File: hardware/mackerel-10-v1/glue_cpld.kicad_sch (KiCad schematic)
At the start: 20 parts, among them J1 Conn_02x05_Odd_Even, J7 Conn_02x03_Odd_Even, X1 50MHz, X2 50MHz

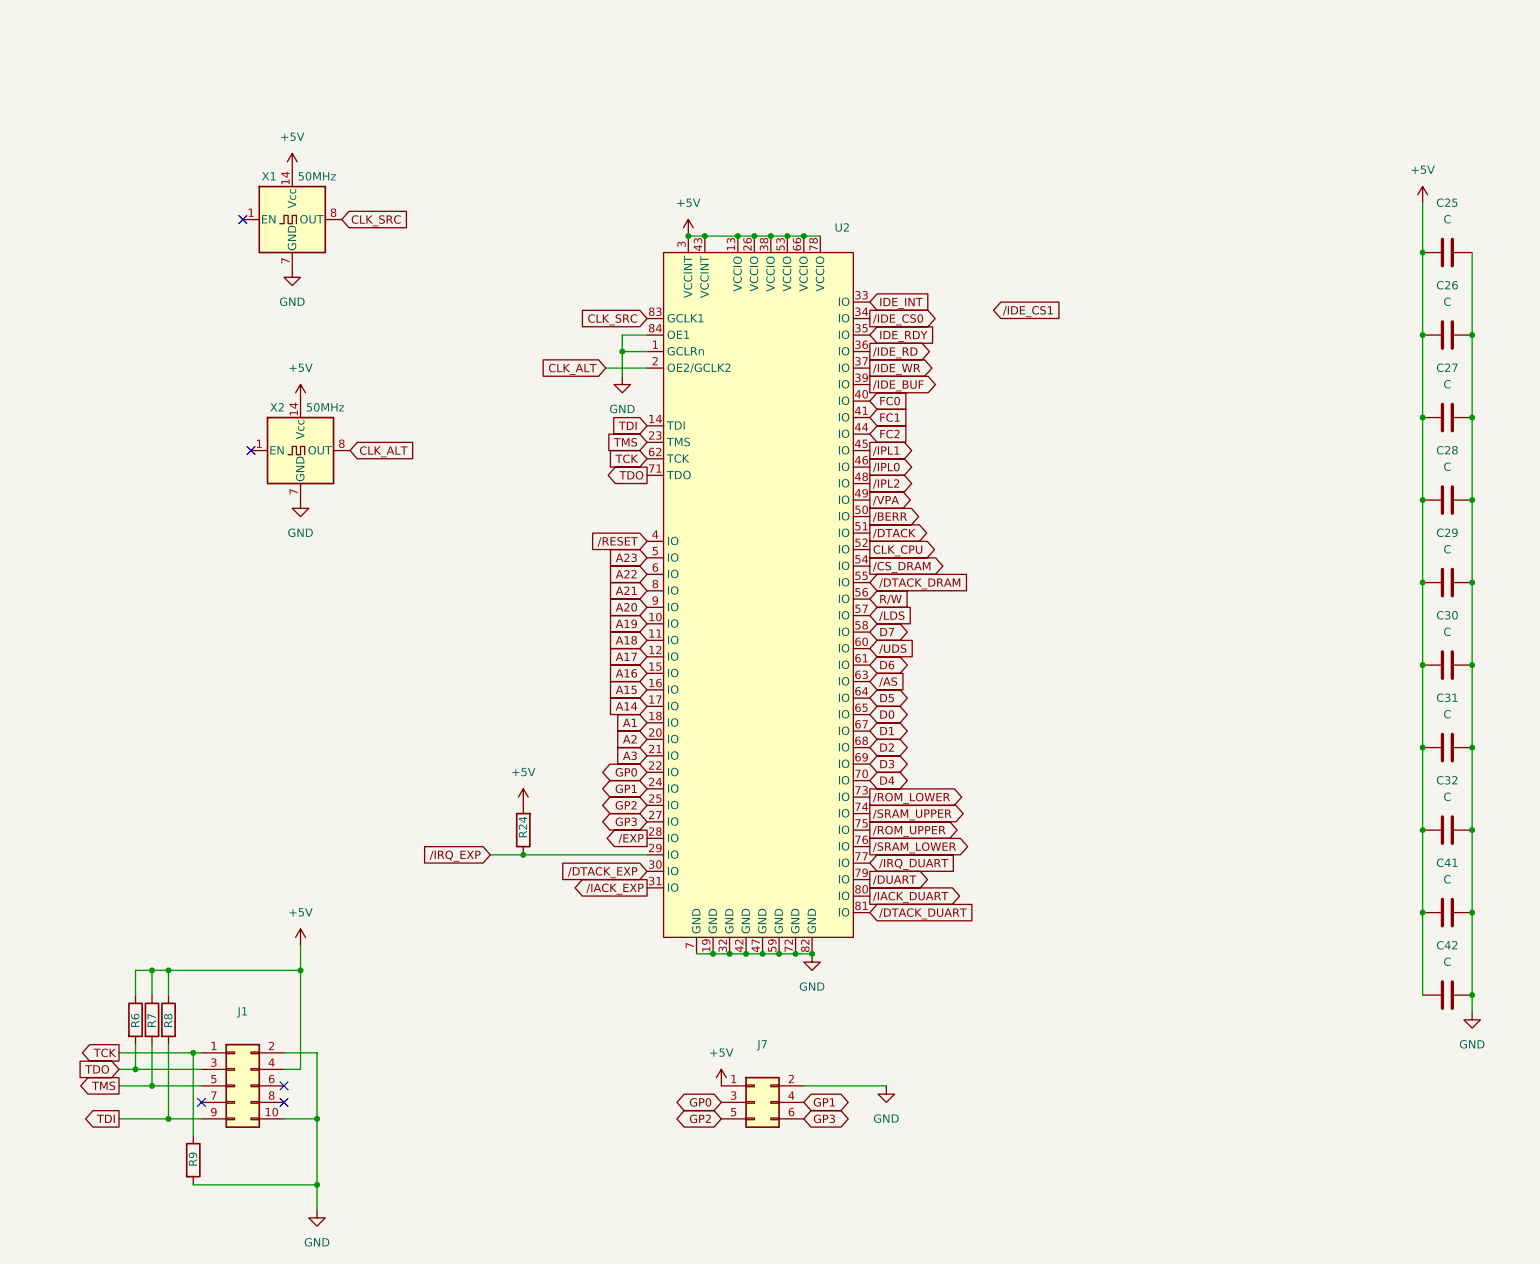
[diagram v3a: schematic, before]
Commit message: Remove BERR from CPLD
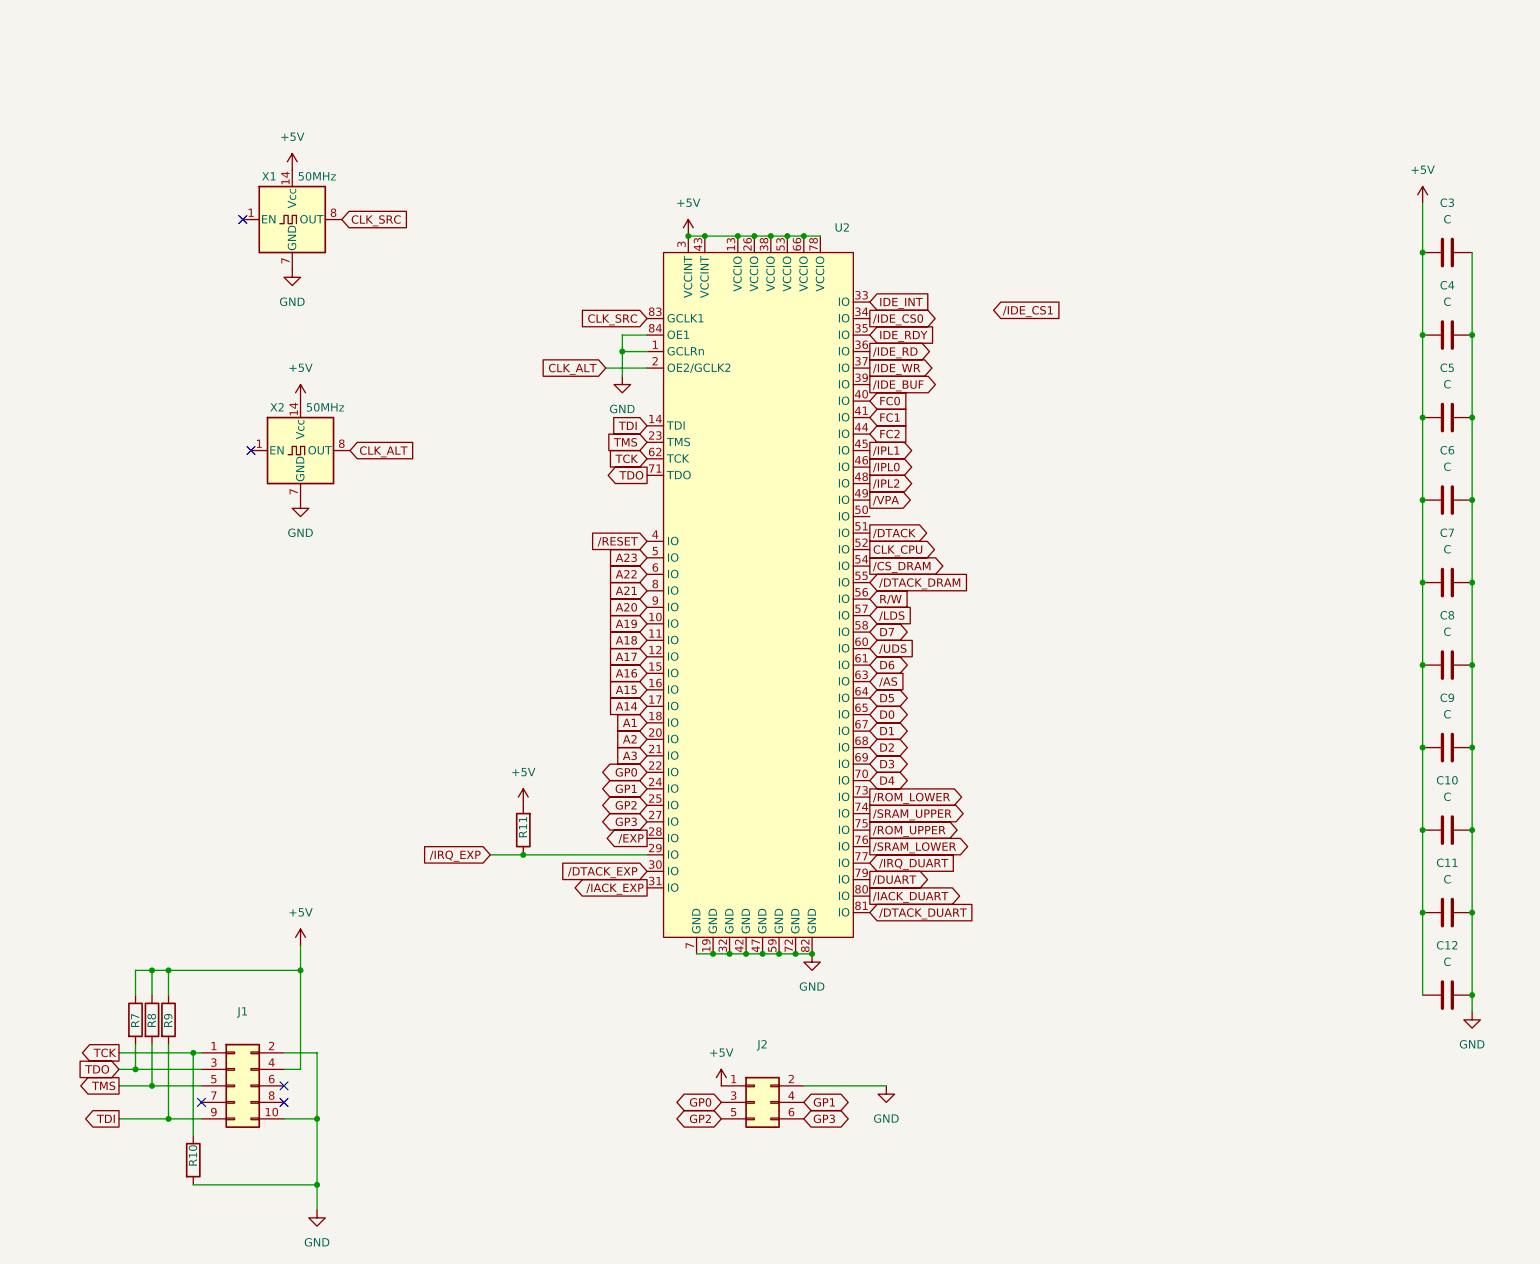
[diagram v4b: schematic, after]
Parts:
- renumbered C32 to C10, C41 to C11, C42 to C12, C25 to C3, C26 to C4, C27 to C5, C28 to C6, C29 to C7, C30 to C8, C31 to C9, J7 to J2, R9 to R10, R24 to R11, R6 to R7, R7 to R8, R8 to R9
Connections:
- net /BERR: no longer names the net of U2.50 (IO)
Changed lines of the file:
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@@
 		)
 	)
-	(global_label "{slash}BERR"
-		(shape output)
-		(at 147.32 81.28 0)
-		(fields_autoplaced yes)
-		(effects
-			(font
-				(size 1.27 1.27)
-			)
-			(justify left)
-		)
-		(property "Intersheetrefs" "${INTERSHEET_REFS}"
-			(at 156.5947 81.28 0)
-			(effects
-				(font
-					(size 1.27 1.27)
-				)
-				(justify left)
-				(hide yes)
-			)
-		)
-	)
 	(global_label "TDI"
 		(shape input)
@@
 		(dnp no)
 		(fields_autoplaced yes)
-		(property "Reference" "#PWR04"
+		(property "Reference" "#PWR010"
 			(at 62.23 194.31 0)
 			(effects
@@
 			(project "mackerel-10-v1"
 				(path "/0a8f74be-008b-4256-a2d9-73a458311ea0/ffc18f07-5f09-466c-bd63-a2a9c38b4664"
-					(reference "#PWR04")
+					(reference "#PWR010")
 					(unit 1)
 				)
@@
 		(dnp no)
 		(fields_autoplaced yes)
-		(property "Reference" "#PWR082"
+		(property "Reference" "#PWR08"
 			(at 59.69 85.09 0)
 			(effects
@@
 			(project "mackerel-10-v1"
 				(path "/0a8f74be-008b-4256-a2d9-73a458311ea0/ffc18f07-5f09-466c-bd63-a2a9c38b4664"
-					(reference "#PWR082")
+					(reference "#PWR08")
 					(unit 1)
 				)
@@
 		(dnp no)
 		(fields_autoplaced yes)
-		(property "Reference" "C26"
+		(property "Reference" "C4"
 			(at 236.22 45.72 90)
 			(effects
@@
 			(project "mackerel-10-v1"
 				(path "/0a8f74be-008b-4256-a2d9-73a458311ea0/ffc18f07-5f09-466c-bd63-a2a9c38b4664"
-					(reference "C26")
+					(reference "C4")
 					(unit 1)
 				)
@@
 		(on_board yes)
 		(dnp no)
-		(property "Reference" "R6"
+		(property "Reference" "R7"
 			(at 34.29 160.02 90)
 			(effects
@@
 			(project "mackerel-10-v1"
 				(path "/0a8f74be-008b-4256-a2d9-73a458311ea0/ffc18f07-5f09-466c-bd63-a2a9c38b4664"
-					(reference "R6")
+					(reference "R7")
 					(unit 1)
 				)
@@
 		(dnp no)
 		(fields_autoplaced yes)
-		(property "Reference" "#PWR067"
+		(property "Reference" "#PWR016"
 			(at 149.86 175.26 0)
 			(effects
@@
 			(project "mackerel-10-v1"
 				(path "/0a8f74be-008b-4256-a2d9-73a458311ea0/ffc18f07-5f09-466c-bd63-a2a9c38b4664"
-					(reference "#PWR067")
+					(reference "#PWR016")
 					(unit 1)
 				)
@@
 		(dnp no)
 		(fields_autoplaced yes)
-		(property "Reference" "C42"
+		(property "Reference" "C12"
 			(at 236.22 147.32 90)
 			(effects
@@
 			(project "mackerel-10-v1"
 				(path "/0a8f74be-008b-4256-a2d9-73a458311ea0/ffc18f07-5f09-466c-bd63-a2a9c38b4664"
-					(reference "C42")
+					(reference "C12")
 					(unit 1)
 				)
@@
 		(dnp no)
 		(fields_autoplaced yes)
-		(property "Reference" "#PWR09"
+		(property "Reference" "#PWR015"
 			(at 138.43 154.94 0)
 			(effects
@@
 			(project "mackerel-10-v1"
 				(path "/0a8f74be-008b-4256-a2d9-73a458311ea0/ffc18f07-5f09-466c-bd63-a2a9c38b4664"
-					(reference "#PWR09")
+					(reference "#PWR015")
 					(unit 1)
 				)
@@
 		(dnp no)
 		(fields_autoplaced yes)
-		(property "Reference" "#PWR088"
+		(property "Reference" "#PWR017"
 			(at 232.41 36.83 0)
 			(effects
@@
 			(project "mackerel-10-v1"
 				(path "/0a8f74be-008b-4256-a2d9-73a458311ea0/ffc18f07-5f09-466c-bd63-a2a9c38b4664"
-					(reference "#PWR088")
+					(reference "#PWR017")
 					(unit 1)
 				)
@@
 		(on_board yes)
 		(dnp no)
-		(property "Reference" "R7"
+		(property "Reference" "R8"
 			(at 36.83 160.02 90)
 			(effects
@@
 			(project "mackerel-10-v1"
 				(path "/0a8f74be-008b-4256-a2d9-73a458311ea0/ffc18f07-5f09-466c-bd63-a2a9c38b4664"
-					(reference "R7")
+					(reference "R8")
 					(unit 1)
 				)
@@
 		(dnp no)
 		(fields_autoplaced yes)
-		(property "Reference" "#PWR0116"
+		(property "Reference" "#PWR011"
 			(at 93.98 129.54 0)
 			(effects
@@
 			(project "mackerel-10-v1"
 				(path "/0a8f74be-008b-4256-a2d9-73a458311ea0/ffc18f07-5f09-466c-bd63-a2a9c38b4664"
-					(reference "#PWR0116")
+					(reference "#PWR011")
 					(unit 1)
 				)
@@
 		(dnp no)
 		(fields_autoplaced yes)
-		(property "Reference" "C28"
+		(property "Reference" "C6"
 			(at 236.22 71.12 90)
 			(effects
@@
 			(project "mackerel-10-v1"
 				(path "/0a8f74be-008b-4256-a2d9-73a458311ea0/ffc18f07-5f09-466c-bd63-a2a9c38b4664"
-					(reference "C28")
+					(reference "C6")
 					(unit 1)
 				)
@@
 		(dnp no)
 		(fields_autoplaced yes)
-		(property "Reference" "C25"
+		(property "Reference" "C3"
 			(at 236.22 33.02 90)
 			(effects
@@
 			(project "mackerel-10-v1"
 				(path "/0a8f74be-008b-4256-a2d9-73a458311ea0/ffc18f07-5f09-466c-bd63-a2a9c38b4664"
-					(reference "C25")
+					(reference "C3")
 					(unit 1)
 				)
@@
 		(on_board yes)
 		(dnp no)
-		(property "Reference" "R24"
+		(property "Reference" "R11"
 			(at 93.98 130.81 90)
 			(effects
@@
 			(project "mackerel-10-v1"
 				(path "/0a8f74be-008b-4256-a2d9-73a458311ea0/ffc18f07-5f09-466c-bd63-a2a9c38b4664"
-					(reference "R24")
+					(reference "R11")
 					(unit 1)
 				)
@@
 		(dnp no)
 		(fields_autoplaced yes)
-		(property "Reference" "J7"
+		(property "Reference" "J2"
 			(at 130.81 162.56 0)
 			(effects
@@
 			(project ""
 				(path "/0a8f74be-008b-4256-a2d9-73a458311ea0/ffc18f07-5f09-466c-bd63-a2a9c38b4664"
-					(reference "J7")
+					(reference "J2")
 					(unit 1)
 				)
@@
 		(on_board yes)
 		(dnp no)
-		(property "Reference" "R8"
+		(property "Reference" "R9"
 			(at 39.37 160.02 90)
 			(effects
@@
 			(project "mackerel-10-v1"
 				(path "/0a8f74be-008b-4256-a2d9-73a458311ea0/ffc18f07-5f09-466c-bd63-a2a9c38b4664"
-					(reference "R8")
+					(reference "R9")
 					(unit 1)
 				)
@@
 		(dnp no)
 		(fields_autoplaced yes)
-		(property "Reference" "C41"
+		(property "Reference" "C11"
 			(at 236.22 134.62 90)
 			(effects
@@
 			(project "mackerel-10-v1"
 				(path "/0a8f74be-008b-4256-a2d9-73a458311ea0/ffc18f07-5f09-466c-bd63-a2a9c38b4664"
-					(reference "C41")
+					(reference "C11")
 					(unit 1)
 				)
@@
 		(dnp no)
 		(fields_autoplaced yes)
-		(property "Reference" "#PWR03"
+		(property "Reference" "#PWR09"
 			(at 59.69 151.13 0)
 			(effects
@@
 			(project "mackerel-10-v1"
 				(path "/0a8f74be-008b-4256-a2d9-73a458311ea0/ffc18f07-5f09-466c-bd63-a2a9c38b4664"
-					(reference "#PWR03")
+					(reference "#PWR09")
 					(unit 1)
 				)
@@
 		(dnp no)
 		(fields_autoplaced yes)
-		(property "Reference" "#PWR068"
+		(property "Reference" "#PWR014"
 			(at 124.46 172.72 0)
 			(effects
@@
 			(project "mackerel-10-v1"
 				(path "/0a8f74be-008b-4256-a2d9-73a458311ea0/ffc18f07-5f09-466c-bd63-a2a9c38b4664"
-					(reference "#PWR068")
+					(reference "#PWR014")
 					(unit 1)
 				)
@@
 		(dnp no)
 		(fields_autoplaced yes)
-		(property "Reference" "C32"
+		(property "Reference" "C10"
 			(at 236.22 121.92 90)
 			(effects
@@
 			(project "mackerel-10-v1"
 				(path "/0a8f74be-008b-4256-a2d9-73a458311ea0/ffc18f07-5f09-466c-bd63-a2a9c38b4664"
-					(reference "C32")
+					(reference "C10")
 					(unit 1)
 				)
@@
 		(dnp no)
 		(fields_autoplaced yes)
-		(property "Reference" "#PWR08"
+		(property "Reference" "#PWR013"
 			(at 119.38 41.91 0)
 			(effects
@@
 			(project "mackerel-10-v1"
 				(path "/0a8f74be-008b-4256-a2d9-73a458311ea0/ffc18f07-5f09-466c-bd63-a2a9c38b4664"
-					(reference "#PWR08")
+					(reference "#PWR013")
 					(unit 1)
 				)
@@
 		(dnp no)
 		(fields_autoplaced yes)
-		(property "Reference" "#PWR07"
+		(property "Reference" "#PWR012"
 			(at 109.22 66.04 0)
 			(effects
@@
 			(project "mackerel-10-v1"
 				(path "/0a8f74be-008b-4256-a2d9-73a458311ea0/ffc18f07-5f09-466c-bd63-a2a9c38b4664"
-					(reference "#PWR07")
+					(reference "#PWR012")
 					(unit 1)
 				)
@@
 		(dnp no)
 		(fields_autoplaced yes)
-		(property "Reference" "#PWR092"
+		(property "Reference" "#PWR018"
 			(at 240.03 163.83 0)
 			(effects
@@
 			(project "mackerel-10-v1"
 				(path "/0a8f74be-008b-4256-a2d9-73a458311ea0/ffc18f07-5f09-466c-bd63-a2a9c38b4664"
-					(reference "#PWR092")
+					(reference "#PWR018")
 					(unit 1)
 				)
@@
 		(dnp no)
 		(fields_autoplaced yes)
-		(property "Reference" "C31"
+		(property "Reference" "C9"
 			(at 236.22 109.22 90)
 			(effects
@@
 			(project "mackerel-10-v1"
 				(path "/0a8f74be-008b-4256-a2d9-73a458311ea0/ffc18f07-5f09-466c-bd63-a2a9c38b4664"
-					(reference "C31")
+					(reference "C9")
 					(unit 1)
 				)
@@
 		(on_board yes)
 		(dnp no)
-		(property "Reference" "R9"
+		(property "Reference" "R10"
 			(at 43.18 181.356 90)
 			(effects
@@
 			(project "mackerel-10-v1"
 				(path "/0a8f74be-008b-4256-a2d9-73a458311ea0/ffc18f07-5f09-466c-bd63-a2a9c38b4664"
-					(reference "R9")
+					(reference "R10")
 					(unit 1)
 				)
@@
 		(dnp no)
 		(fields_autoplaced yes)
-		(property "Reference" "C30"
+		(property "Reference" "C8"
 			(at 236.22 96.52 90)
 			(effects
@@
 			(project "mackerel-10-v1"
 				(path "/0a8f74be-008b-4256-a2d9-73a458311ea0/ffc18f07-5f09-466c-bd63-a2a9c38b4664"
-					(reference "C30")
+					(reference "C8")
 					(unit 1)
 				)
@@
 		(on_board yes)
 		(dnp no)
-		(property "Reference" "C27"
+		(property "Reference" "C5"
 			(at 236.22 58.42 90)
 			(effects
@@
 			(project "mackerel-10-v1"
 				(path "/0a8f74be-008b-4256-a2d9-73a458311ea0/ffc18f07-5f09-466c-bd63-a2a9c38b4664"
-					(reference "C27")
+					(reference "C5")
 					(unit 1)
 				)
@@
 		(dnp no)
 		(fields_autoplaced yes)
-		(property "Reference" "#PWR081"
+		(property "Reference" "#PWR07"
 			(at 59.69 67.31 0)
 			(effects
@@
 			(project "mackerel-10-v1"
 				(path "/0a8f74be-008b-4256-a2d9-73a458311ea0/ffc18f07-5f09-466c-bd63-a2a9c38b4664"
-					(reference "#PWR081")
+					(reference "#PWR07")
 					(unit 1)
 				)
@@
 		(dnp no)
 		(fields_autoplaced yes)
-		(property "Reference" "C29"
+		(property "Reference" "C7"
 			(at 236.22 83.82 90)
 			(effects
@@
 			(project "mackerel-10-v1"
 				(path "/0a8f74be-008b-4256-a2d9-73a458311ea0/ffc18f07-5f09-466c-bd63-a2a9c38b4664"
-					(reference "C29")
+					(reference "C7")
 					(unit 1)
 				)

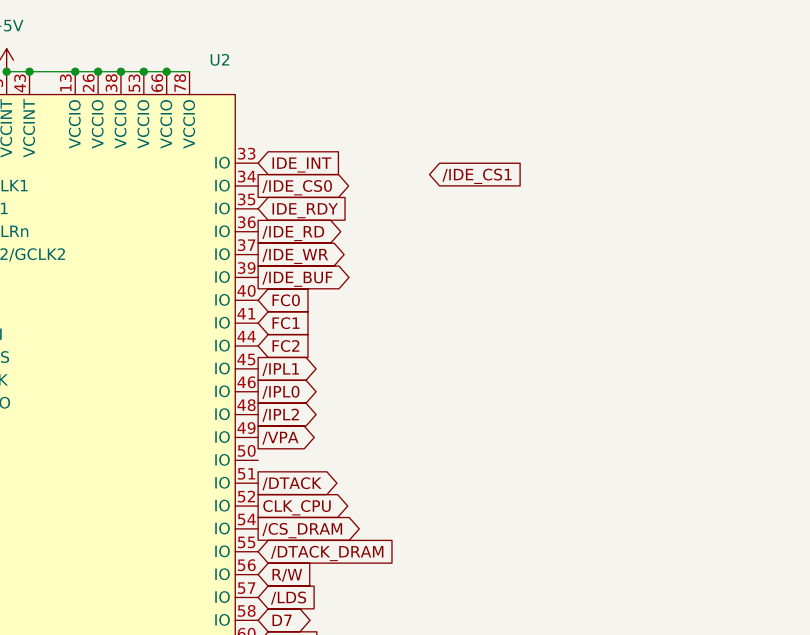
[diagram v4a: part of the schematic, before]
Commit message: Rearranged power and reset on PCB
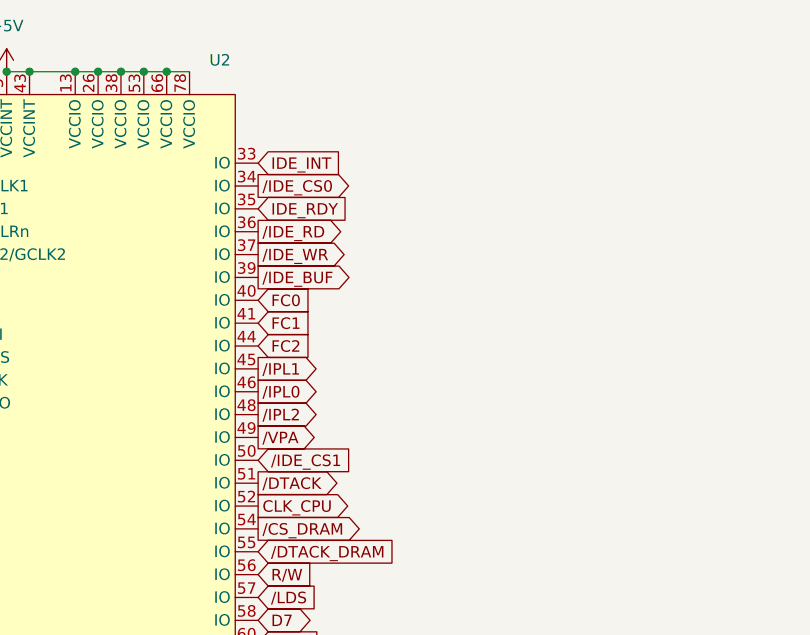
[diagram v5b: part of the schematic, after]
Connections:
- net /IDE_CS1: now also U2.50 (IO)
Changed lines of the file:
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@@
 	(global_label "{slash}IDE_CS1"
 		(shape input)
-		(at 166.37 49.53 0)
+		(at 147.32 81.28 0)
 		(fields_autoplaced yes)
 		(effects
@@
 		)
 		(property "Intersheetrefs" "${INTERSHEET_REFS}"
-			(at 178.3661 49.53 0)
+			(at 159.3161 81.28 0)
 			(effects
 				(font

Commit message: Mackerel-10 v1.1 release PCB
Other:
- title: Mackerel-10 SBC v1 -> Mackerel-10 SBC v1.1
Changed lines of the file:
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@@
 	(paper "A")
 	(title_block
-		(title "Mackerel-10 SBC v1")
-		(date "2024-09-23")
-		(rev "1.0a")
+		(title "Mackerel-10 SBC v1.1")
+		(date "2024-10-27")
+		(rev "1.1a")
 		(company "Colin Maykish")
 	)

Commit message: Add Mackerel-10 v1.1 BOM
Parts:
- C10, C11, C12, C3, C4, C5, C6, C7, C8, C9: value C -> 0.1uF
- R10, R11, R7, R8, R9: value R -> 4k7
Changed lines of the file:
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@@
 			)
 		)
-		(property "Value" "C"
+		(property "Value" "0.1uF"
 			(at 236.22 48.26 90)
 			(effects
@@
 			)
 		)
-		(property "Value" "R"
+		(property "Value" "4k7"
 			(at 36.83 160.0199 0)
 			(effects
@@
 			)
 		)
-		(property "Value" "C"
+		(property "Value" "0.1uF"
 			(at 236.22 149.86 90)
 			(effects
@@
 			)
 		)
-		(property "Value" "R"
+		(property "Value" "4k7"
 			(at 39.37 160.0199 0)
 			(effects
@@
 			)
 		)
-		(property "Value" "C"
+		(property "Value" "0.1uF"
 			(at 236.22 73.66 90)
 			(effects
@@
 			)
 		)
-		(property "Value" "C"
+		(property "Value" "0.1uF"
 			(at 236.22 35.56 90)
 			(effects
@@
 			)
 		)
-		(property "Value" "R"
+		(property "Value" "4k7"
 			(at 91.44 130.81 0)
 			(effects
@@
 			)
 		)
-		(property "Value" "R"
+		(property "Value" "4k7"
 			(at 41.91 160.0199 0)
 			(effects
@@
 			)
 		)
-		(property "Value" "C"
+		(property "Value" "0.1uF"
 			(at 236.22 137.16 90)
 			(effects
@@
 			)
 		)
-		(property "Value" "C"
+		(property "Value" "0.1uF"
 			(at 236.22 124.46 90)
 			(effects
@@
 			)
 		)
-		(property "Value" "C"
+		(property "Value" "0.1uF"
 			(at 236.22 111.76 90)
 			(effects
@@
 			)
 		)
-		(property "Value" "R"
+		(property "Value" "4k7"
 			(at 45.72 181.6099 0)
 			(effects
@@
 			)
 		)
-		(property "Value" "C"
+		(property "Value" "0.1uF"
 			(at 236.22 99.06 90)
 			(effects
@@
 			)
 		)
-		(property "Value" "C"
+		(property "Value" "0.1uF"
 			(at 236.22 60.96 90)
 			(effects
@@
 			)
 		)
-		(property "Value" "C"
+		(property "Value" "0.1uF"
 			(at 236.22 86.36 90)
 			(effects

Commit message: Mackerel-10 v1.2 Gerber release
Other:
- title: Mackerel-10 SBC v1.1 -> Mackerel-10
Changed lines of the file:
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@@
 	(paper "A")
 	(title_block
-		(title "Mackerel-10 SBC v1.1")
-		(date "2024-10-27")
-		(rev "1.1a")
+		(title "Mackerel-10")
+		(date "2024-11-09")
+		(rev "1.2")
 		(company "Colin Maykish")
 	)
